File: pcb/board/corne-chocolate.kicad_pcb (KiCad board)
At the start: 2 copper layers, 236.4 x 101.8 mm, 164 parts, among them J1 Conn_01x04, J2 54-00174, J3 781271220, J4 54-00174, J5 Conn_01x04, P1 Conn_01x01, P2 Conn_01x01, SW1 SW_PUSH, SW10 SW_PUSH, SW11 SW_PUSH, SW12 SW_PUSH, SW13 SW_PUSH, SW14 SW_PUSH, SW15 SW_PUSH, SW16 SW_PUSH, SW17 SW_PUSH, SW18 SW_PUSH, SW19 SW_PUSH, SW2 SW_PUSH, SW20 SW_PUSH, SW21 SW_PUSH, SW22 SW_PUSH, SW23 SW_PUSH, SW24 SW_PUSH, SW25 SW_PUSH, SW26 SW_PUSH, SW27 SW_PUSH, SW28 SW_PUSH, SW29 SW_PUSH, SW3 SW_PUSH, SW30 SW_PUSH, SW31 SW_PUSH, SW32 SW_PUSH, SW33 SW_PUSH, SW34 SW_PUSH, SW35 SW_PUSH, SW36 SW_PUSH, SW4 SW_PUSH, SW5 SW_PUSH, SW6 SW_PUSH, SW7 SW_PUSH, SW8 SW_PUSH, SW9 SW_PUSH, U1 ProMicro, U2 ProMicro

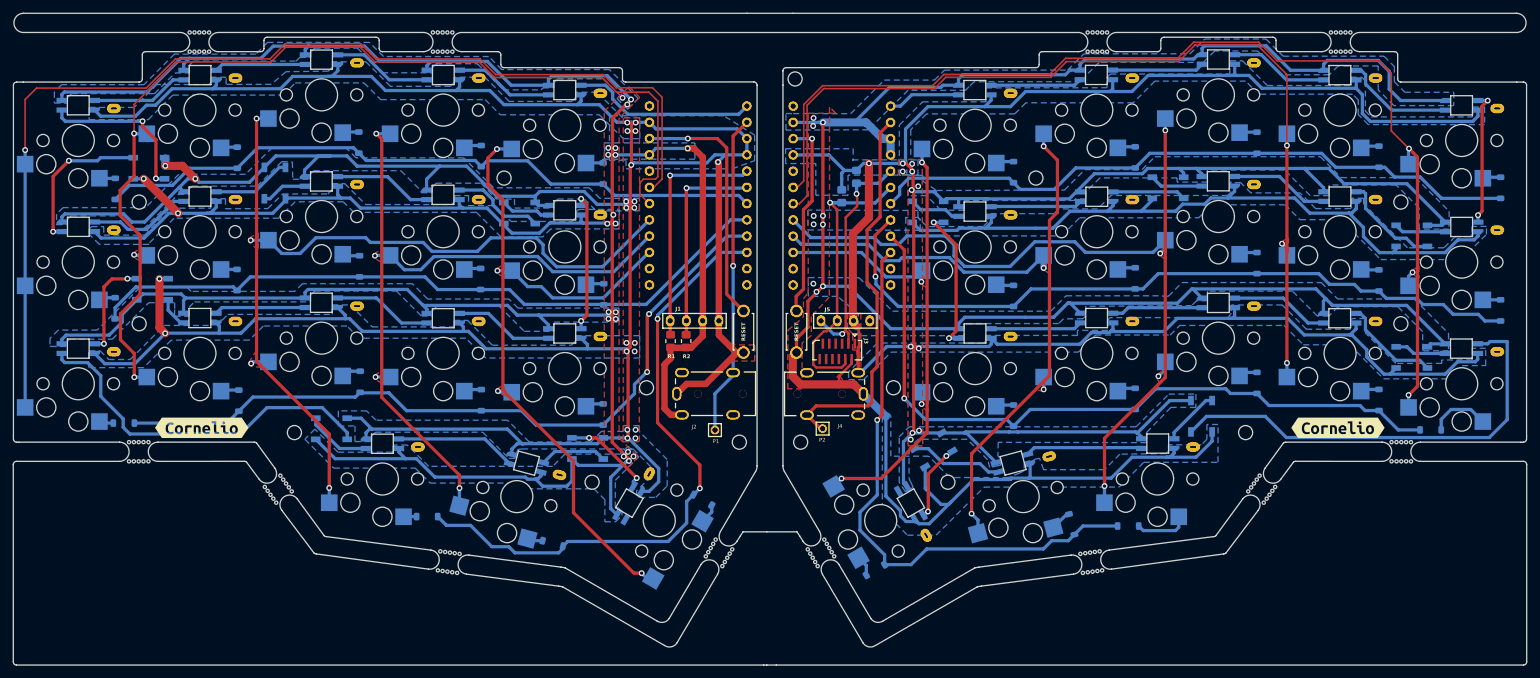
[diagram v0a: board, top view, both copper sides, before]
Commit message: new board shape
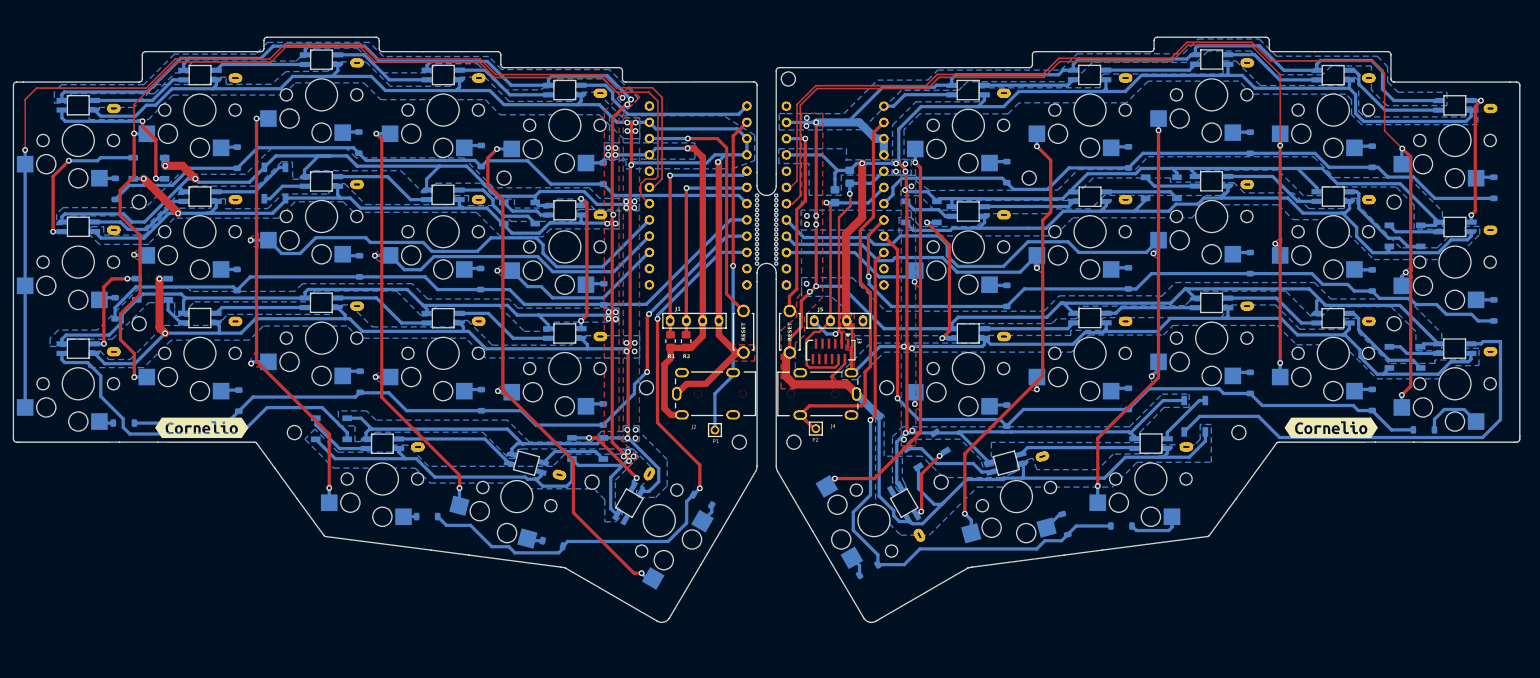
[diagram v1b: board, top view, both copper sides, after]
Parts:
- removed the mouse-bite-3mm-slot at (70.9, 127.7)
- removed the mouse-bite-3mm-slot at (236.8, 57.9)
- removed the mouse-bite-3mm-slot at (246.3, 121.8)
- removed the mouse-bite-3mm-slot at (155.7, 137.6)
- removed the mouse-bite-3mm-slot at (58.5, 57.9)
- removed the mouse-bite-3mm-slot at (97.5, 139.1)
- removed the mouse-bite-3mm-slot at (96.5, 57.9)
- removed the mouse-bite-3mm-slot at (49.1, 121.8)
- removed the mouse-bite-3mm-slot at (139.7, 137.7)
- removed the mouse-bite-3mm-slot at (197.9, 139.1)
- removed the mouse-bite-3mm-slot at (224.5, 127.7)
- removed the mouse-bite-3mm-slot at (198.8, 57.9)
- added mouse-bite-3mm-slot: VAL**, kbd:mouse-bite-3mm-slot, B.Cu at (147.2, 90.9)
- moved D21 1.05 mm to (222.7, 73.6)
- moved D26 1.05 mm to (222.7, 92.4)
- moved D29 1.05 mm to (249.8, 118.4)
- moved D31 1.05 mm to (222.7, 111.1)
- moved D34 1.05 mm to (202.6, 133.5)
- moved D35 1.05 mm to (193.8, 133.2)
- moved D36 1.05 mm to (163.1, 140.3)
- moved H10 1.05 mm to (220.9, 118.9)
- moved H11 1.05 mm to (245.2, 101.9)
- moved H12 1.05 mm to (245.2, 82.9)
- moved H13 1.05 mm to (188.2, 79.1)
- moved H14 1.05 mm to (174.4, 126.6)
- moved H15 1.05 mm to (150.6, 63.6)
- moved H8 1.05 mm to (151.4, 120.4)
- moved H9 1.05 mm to (165.9, 111.9)
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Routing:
- net RSCL: track 46.0 -> 45.1 mm
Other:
- board size 236.4 x 101.8 mm -> 235.3 x 91.4 mm
